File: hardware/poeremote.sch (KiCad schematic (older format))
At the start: 65 parts, among them J1 3.3VDC, J2 48VDC, J3 RJ45, J4 SERIAL, J5 ISP, J6 CONN_7, J7 LAMP, P4 J?, Q1 SOT23-BEC, Q2 PNP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

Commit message: Reworking hardware into wall-switch version
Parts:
- removed J6: CONN_7, symbol CONN_7
- removed P4: J?, symbol CONN_5
- removed R43, R44: 270, symbol R
- added C10: 15uF, symbol C
- added C34: 1uf, symbol C
- added C?: 0.1uF, symbol C
- added K1: RT314024, relay-RT-C/O16A5, symbol RT314024
- added K2: CONN_3, symbol CONN_3
- added P1: CONN_2, symbol CONN_2
- added P2: CONN_10, symbol CONN_10
- added R53, R54: 47k, symbol R
- added R55: 60K, symbol R
- added Sw1, Sw2: SPST-D, symbol SPST-D
- added U6: RE200B, symbol RE200B
- added U7: ZEPIR0AAS02MOD, symbol ZEPIR0AAS02MOD
- added U8: GA1A1S, symbol GA1A1S
- C24, C6, C8: Voltage (none) -> 16V
- C4, C5: Voltage (none) -> 100V
- C9: value 15uF -> 100nF; Voltage (none) -> 100V
- R17: value 8.66K -> 5.6K
- R3: value 2.87K -> 9.424K
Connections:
- net labels added: EXT_PA2, EXT_PA3, EXT_PC4, EXT_PC5, EXT_PC6, EXT_PC7, EXT_PD0, EXT_PD1, EXT_PD2, LIGHT_V, PIR_RX, PIR_TX, sw_bottom, sw_top
- net labels removed: SR1, SR2, SR3, SR4, VCC
- wire segments 236 -> 255
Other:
- moved on the sheet: J2

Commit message: Modified the board to use correctly-sized components, re-laid it out to fit in as a light switch, upgraded to a newer version of KiCad, and used an extra field in KiCad to indicate the Mouser part number for most of the parts
The end result is that building a BOM is much easier now, to the point that you can order from mouser directly from the auto-generated BOM.
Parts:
- removed U5: XMEGA A4, symbol XMEGA~A4
- added D3, D4: LED, symbol LED
- added R56, R57: 10, symbol R
- added U5: XMEGA-A4, symbol XMEGA-A4
- C10: Mouser Part Number (none) -> 647-UUR2A220MNL1GS
- C12: footprint (none) -> SM0603; Mouser Part Number (none) -> 581-06031C102K; Voltage (none) -> 100
- C13, C14, C15, C16, C17, C18, C19, C20: Mouser Part Number (none) -> 581-06031C102K
- C21: Mouser Part Number (none) -> 603-CC805MKX5R5BB226; Voltage (none) -> 6.3V
- C22: Mouser Part Number (none) -> 77-VJ0603Y332KXACBC; Voltage (none) -> 16
- C23: Mouser Part Number (none) -> 77-VJ0603Y332KXACBC; Voltage (none) -> 16V
- C24: Mouser Part Number (none) -> 810-C1608X5R1C334K
- C25: Mouser Part Number (none) -> 598-AVE108M10G24T-F; Voltage (none) -> 6.3V
- C27, C28, C29, C33: Mouser Part Number (none) -> 581-060316C104K
- C30: Mouser Part Number (none) -> 603-CC603MRX5R5BB106
- C31, C32: Mouser Part Number (none) -> 810-C1608C0G1H180J
- C34: Mouser Part Number (none) -> 77-VJ0603V105MXQPBC
- C35: renamed from C?; Mouser Part Number (none) -> 581-060316C104K
- C4, C5, C9: Mouser Part Number (none) -> 603-CC206KKX7R0BB104
- C6: Mouser Part Number (none) -> 77-VJ0603V104ZXAPBC
- C8: Mouser Part Number (none) -> 77-VJ0603Y151KXACBC
- D1: Mouser Part Number (none) -> 863-MBRS1100T3G
- D2: Mouser Part Number (none) -> 625-BZT52C5V1-V
- J3: Mouser Part Number (none) -> 523-RJHSE-3081
- J5: Mouser Part Number (none) -> 649-78548-406HLF
- L1, L3: Mouser Part Number (none) -> 81-BLM21P300S
- L2: Mouser Part Number (none) -> 652-SDR0805-330KL
- Q1: Mouser Part Number (none) -> 512-MMBT3904
- Q2: Mouser Part Number (none) -> 771-BCW89215
- R1: Mouser Part Number (none) -> 667-ERJ-3EKF1002V
- R10: Mouser Part Number (none) -> 667-ERJ-3EKF3012V
- R11: Mouser Part Number (none) -> 302-45.3-RC
- R12: Mouser Part Number (none) -> 301-5.1-RC
- R17: value 5.6K -> 9.424K; Mouser Part Number (none) -> 667-ERJ-3EKF9531V
- R3: value 9.424K -> 5.6K; Mouser Part Number (none) -> 279-CFR25J5K6
- R40: Mouser Part Number (none) -> 302-2.32K-RC
- R41, R42: Mouser Part Number (none) -> 301-220-RC
- R45: value 270 -> 220; Mouser Part Number (none) -> 301-220-RC
- R47, R48, R49, R50: Mouser Part Number (none) -> 301-51-RC
- R51: value 100K -> 25.5k; Mouser Part Number (none) -> 667-ERJ-3EKF2552V
- R52: value 50K -> 25.5k; Mouser Part Number (none) -> 667-ERJ-3EKF2552V
- R53, R54: Mouser Part Number (none) -> 667-ERJ-3GEYJ473V
- R55: value 60K -> 47k; Mouser Part Number (none) -> 667-ERJ-3GEYJ473V
- R6: Mouser Part Number (none) -> 667-ERJ-3EKF2552V
- Sw1, Sw2: Mouser Part Number (none) -> 101-0624-EV
- T1: Mouser Part Number (none) -> 871-B78476A8248A3
- U3: Mouser Part Number (none) -> 634-SI3402-A-GM
- U4: Mouser Part Number (none) -> 579-ENC28J60-I/SS
- U6: Mouser Part Number (none) -> -
- U7: Mouser Part Number (none) -> 692-ZMOT0BSB1A0CG
- U8: Mouser Part Number (none) -> 852-GA1A1S202WP
- X1: Mouser Part Number (none) -> 815-ABM3C-25-D4YT
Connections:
- net labels added: EXT_PB3, SLED1, SLED2
- wire segments 255 -> 258

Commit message: Fixed the PIR motion nsensor
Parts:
- removed R53: 47k, symbol R
- removed U7: ZEPIR0AAS02MOD, symbol ZEPIR0AAS02MOD
- added C11, C3: 10uf, symbol C
- added C2: 100uF, symbol C
- added C26, C7: 10nF, symbol C
- added R13, R14: 100k, symbol R
- added R15, R7: 1M, symbol R
- added R4, R5, R8, R9: 10k, symbol R
- added U1: LM358, symbol LM358
- C1: renamed from C34; value 1uf -> 10uf
- renumbered R54 to R2
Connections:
- net labels added: EXT_PC2, EXT_PC3, MOT_NEG, MOT_POS
- net labels removed: PIR_RX, PIR_TX
- wire segments 258 -> 281
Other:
- moved on the sheet: C1, R2, U6

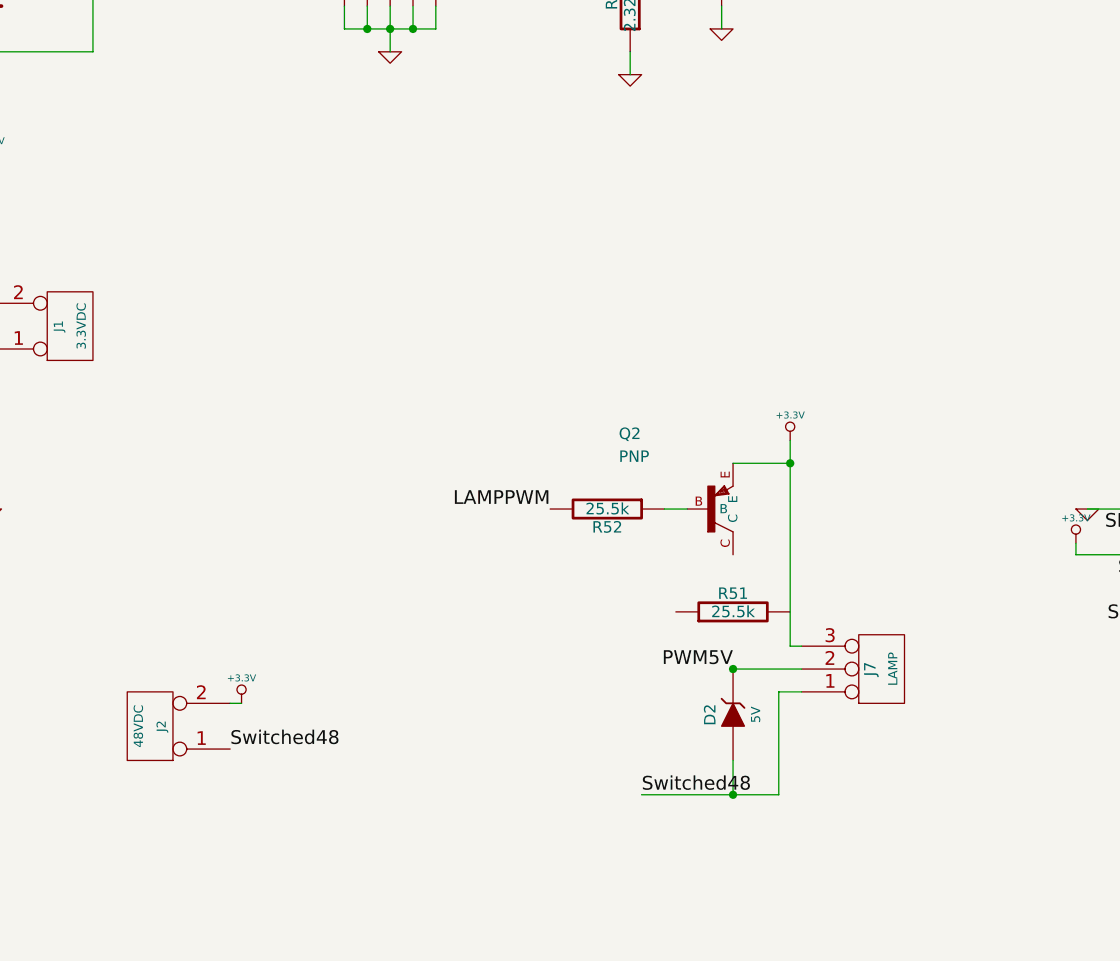
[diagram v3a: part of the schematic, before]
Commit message: Redid the board to include an open-loop mini dc-dc converter run by the xmega
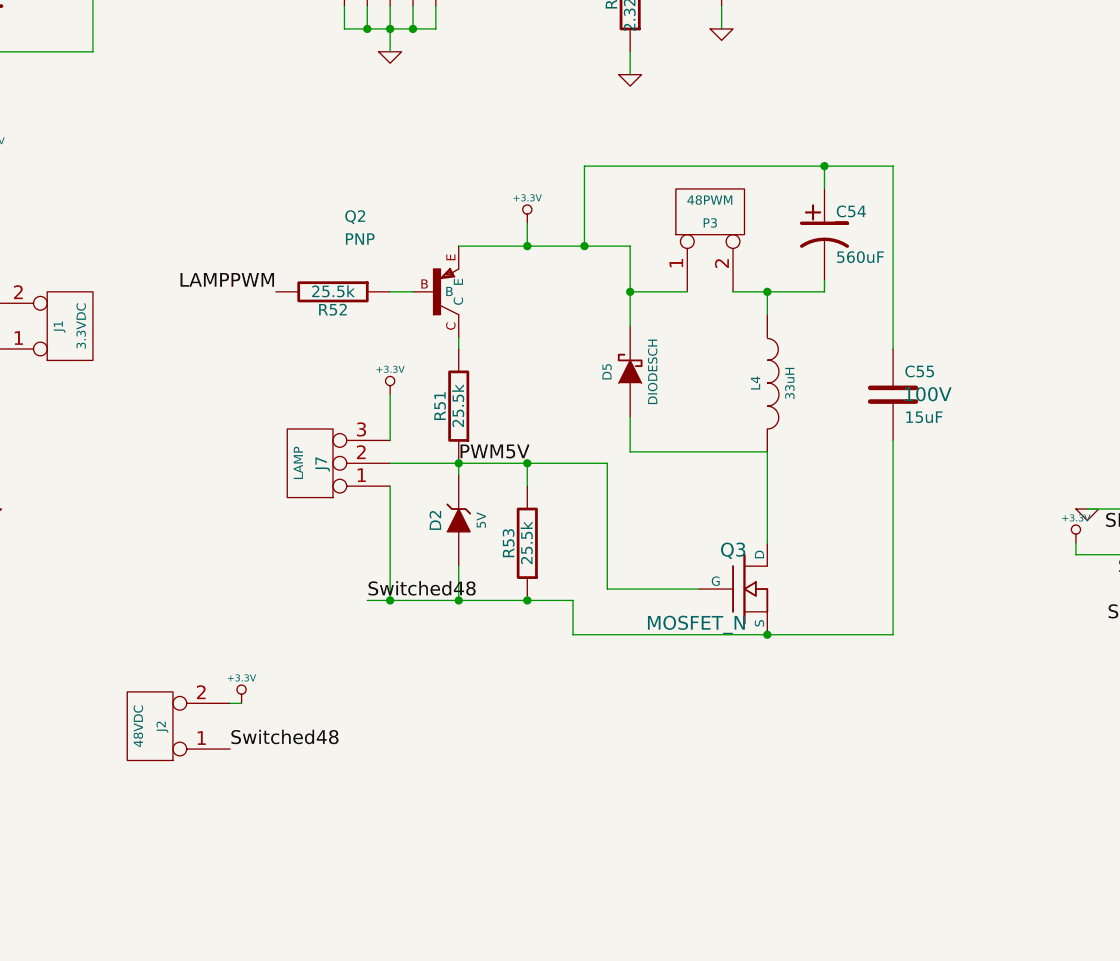
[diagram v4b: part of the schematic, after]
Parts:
- added C54: 560uF, symbol CP1
- added C55: 15uF, symbol C
- added D5: DIODESCH, symbol DIODESCH
- added L4: 33uH, symbol INDUCTOR
- added P3: 48PWM, symbol CONN_2
- added Q3: MOSFET_N, symbol MOSFET_N
- added R53: 25.5k, symbol R
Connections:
- wire segments 281 -> 300
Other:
- moved on the sheet: D2, J7, Q2, R51, R52

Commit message: changes to the schematic, not yet in board.
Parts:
- removed R45: 220, symbol R
- C1, C11, C3: Mouser Part Number 77-VJ0603V105MXQPBC -> 603-CC603MRX5R5BB106
- C2: value 100uF -> 22uF; Mouser Part Number 77-VJ0603V105MXQPBC -> 810-C1608X5R0J226M
- C25: Mouser Part Number 598-AVE108M10G24T-F -> 647-UCD0J102MNL1GS
- C26, C7: Mouser Part Number 77-VJ0603V105MXQPBC -> GRM188R71H103JA01D
- Q3: Mouser Part Number (none) -> 942-IRLML2060TRPBF
- R13, R14: Mouser Part Number 667-ERJ-3GEYJ473V -> 603-AC0603JR-07100KL
- R15, R7: Mouser Part Number 667-ERJ-3GEYJ473V -> 603-AC0603JR-071ML
- R17: value 9.424K -> 3.327K
- R4, R5, R8, R9: Mouser Part Number 667-ERJ-3GEYJ473V -> 667-ERJ-3EKF1002V
- U1: Mouser Part Number (none) -> 595-LM358ADRE4
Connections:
- net labels added: ETHCS
- net labels removed: ETHEN
- wire segments 300 -> 299
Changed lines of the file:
@@
-EESchema Schematic File Version 2  date Sun 08 Jul 2012 11:13:59 PM EDT
+EESchema Schematic File Version 2  date Sat 26 Jan 2013 07:09:22 PM EST
 LIBS:power
 LIBS:device
@@
 EELAYER END
 $Descr A4 11700 8267
-encoding utf-8
 Sheet 1 1
 Title ""
-Date "9 jul 2012"
+Date "27 jan 2013"
 Rev ""
 Comp ""
@@
 Comment4 ""
 $EndDescr
+Text Label 16000 2250 0    60   ~ 0
+ETHCS
 Connection ~ 10500 4850
 Wire Wire Line
@@
 Wire Wire Line
 	9750 2900 10050 2900
-Wire Wire Line
-	10550 2850 10550 2900
 Wire Wire Line
 	10300 3600 10300 3700
@@
 F 0 "Q3" H 10410 6320 60  0000 R CNN
 F 1 "MOSFET_N" H 10410 6000 60  0000 R CNN
+F 4 "942-IRLML2060TRPBF" H 10400 6150 60  0001 C CNN "Mouser Part Number"
 	1    10400 6150
 	1    0    0    -1
@@
 F 0 "C26" H 23500 3950 50  0000 L CNN
 F 1 "10nF" H 23500 3750 50  0000 L CNN
-F 4 "77-VJ0603V105MXQPBC" H 23450 3850 60  0001 C CNN "Mouser Part Number"
+F 4 "GRM188R71H103JA01D" H 23450 3850 60  0001 C CNN "Mouser Part Number"
 	1    23450 3850
 	0    -1   -1   0
@@
 F 0 "R15" V 23530 3550 50  0000 C CNN
 F 1 "1M" V 23450 3550 50  0000 C CNN
-F 4 "667-ERJ-3GEYJ473V" H 23450 3550 60  0001 C CNN "Mouser Part Number"
+F 4 "603-AC0603JR-071ML" H 23450 3550 60  0001 C CNN "Mouser Part Number"
 	1    23450 3550
 	0    -1   1    0
@@
 F 0 "R13" V 22530 2800 50  0000 C CNN
 F 1 "100k" V 22450 2800 50  0000 C CNN
-F 4 "667-ERJ-3GEYJ473V" H 22450 2800 60  0001 C CNN "Mouser Part Number"
+F 4 "603-AC0603JR-07100KL" H 22450 2800 60  0001 C CNN "Mouser Part Number"
 	1    22450 2800
 	-1   0    0    -1
@@
 F 0 "R14" V 22530 3800 50  0000 C CNN
 F 1 "100k" V 22450 3800 50  0000 C CNN
-F 4 "667-ERJ-3GEYJ473V" H 22450 3800 60  0001 C CNN "Mouser Part Number"
+F 4 "603-AC0603JR-07100KL" H 22450 3800 60  0001 C CNN "Mouser Part Number"
 	1    22450 3800
 	-1   0    0    -1
@@
 F 0 "R9" V 21930 3900 50  0000 C CNN
 F 1 "10k" V 21850 3900 50  0000 C CNN
-F 4 "667-ERJ-3GEYJ473V" H 21850 3900 60  0001 C CNN "Mouser Part Number"
+F 4 "667-ERJ-3EKF1002V" H 21850 3900 60  0001 C CNN "Mouser Part Number"
 	1    21850 3900
 	-1   0    0    -1
@@
 F 0 "R8" V 21930 3300 50  0000 C CNN
 F 1 "10k" V 21850 3300 50  0000 C CNN
-F 4 "667-ERJ-3GEYJ473V" H 21850 3300 60  0001 C CNN "Mouser Part Number"
+F 4 "667-ERJ-3EKF1002V" H 21850 3300 60  0001 C CNN "Mouser Part Number"
 	1    21850 3300
 	-1   0    0    -1
@@
 F 0 "R7" V 21430 3600 50  0000 C CNN
 F 1 "1M" V 21350 3600 50  0000 C CNN
-F 4 "667-ERJ-3GEYJ473V" H 21350 3600 60  0001 C CNN "Mouser Part Number"
+F 4 "603-AC0603JR-071ML" H 21350 3600 60  0001 C CNN "Mouser Part Number"
 	1    21350 3600
 	0    -1   1    0
@@
 F 0 "C7" H 21400 4050 50  0000 L CNN
 F 1 "10nF" H 21400 3850 50  0000 L CNN
-F 4 "77-VJ0603V105MXQPBC" H 21350 3950 60  0001 C CNN "Mouser Part Number"
+F 4 "GRM188R71H103JA01D" H 21350 3950 60  0001 C CNN "Mouser Part Number"
 	1    21350 3950
 	0    -1   -1   0
@@
 F 0 "C3" H 20600 4100 50  0000 L CNN
 F 1 "10uf" H 20600 3900 50  0000 L CNN
-F 4 "77-VJ0603V105MXQPBC" H 20550 4000 60  0001 C CNN "Mouser Part Number"
+F 4 "603-CC603MRX5R5BB106" H 20550 4000 60  0001 C CNN "Mouser Part Number"
 	1    20550 4000
 	1    0    0    -1
@@
 F 0 "R5" V 20630 3550 50  0000 C CNN
 F 1 "10k" V 20550 3550 50  0000 C CNN
-F 4 "667-ERJ-3GEYJ473V" H 20550 3550 60  0001 C CNN "Mouser Part Number"
+F 4 "667-ERJ-3EKF1002V" H 20550 3550 60  0001 C CNN "Mouser Part Number"
 	1    20550 3550
 	-1   0    0    -1
@@
 F 0 "C11" H 22100 3500 50  0000 L CNN
 F 1 "10uf" H 22100 3300 50  0000 L CNN
-F 4 "77-VJ0603V105MXQPBC" H 22050 3400 60  0001 C CNN "Mouser Part Number"
+F 4 "603-CC603MRX5R5BB106" H 22050 3400 60  0001 C CNN "Mouser Part Number"
 	1    22050 3400
 	1    0    0    -1
@@
 F 0 "R4" V 20030 2450 50  0000 C CNN
 F 1 "10k" V 19950 2450 50  0000 C CNN
-F 4 "667-ERJ-3GEYJ473V" H 19950 2450 60  0001 C CNN "Mouser Part Number"
+F 4 "667-ERJ-3EKF1002V" H 19950 2450 60  0001 C CNN "Mouser Part Number"
 	1    19950 2450
 	0    -1   1    0
@@
 P 20200 2650
 F 0 "C2" H 20250 2750 50  0000 L CNN
-F 1 "100uF" H 20250 2550 50  0000 L CNN
-F 4 "77-VJ0603V105MXQPBC" H 20200 2650 60  0001 C CNN "Mouser Part Number"
+F 1 "22uF" H 20250 2550 50  0000 L CNN
+F 4 "810-C1608X5R0J226M" H 20200 2650 60  0001 C CNN "Mouser Part Number"
 	1    20200 2650
 	1    0    0    -1
@@
 F 0 "U1" H 21000 3250 60  0000 L CNN
 F 1 "LM358" H 21000 2800 60  0000 L CNN
+F 4 "595-LM358ADRE4" H 21050 3050 60  0001 C CNN "Mouser Part Number"
 	1    21050 3050
 	1    0    0    -1
@@
 Text Label 16000 2550 0    60   ~ 0
 EXT_PD1
-Text Label 16000 2450 0    60   ~ 0
+Text Label 16700 2400 0    60   ~ 0
 EXT_PD2
 Text Label 16650 5700 2    60   ~ 0
@@
 	1    0    0    -1
 $EndComp
-Text Label 16000 2350 0    60   ~ 0
+Text Label 16000 2450 0    60   ~ 0
 sw_bottom
 Text Label 13800 750  1    60   ~ 0
@@
 F 0 "C1" H 19750 2750 50  0000 L CNN
 F 1 "10uf" H 19750 2550 50  0000 L CNN
-F 4 "77-VJ0603V105MXQPBC" H 19700 2650 60  0001 C CNN "Mouser Part Number"
+F 4 "603-CC603MRX5R5BB106" H 19700 2650 60  0001 C CNN "Mouser Part Number"
 	1    19700 2650
 	1    0    0    -1
@@
 F 1 "+3.3V" H 8850 1910 30  0000 C CNN
 	1    8850 1800
-	1    0    0    -1
-$EndComp
-$Comp
-L +3.3V #PWR023
-U 1 1 4E781610
-P 10550 2850
-F 0 "#PWR023" H 10550 2810 30  0001 C CNN
-F 1 "+3.3V" H 10550 2960 30  0000 C CNN
-	1    10550 2850
 	1    0    0    -1
 $EndComp
@@
 Text Label 10550 2350 0    60   ~ 0
 ETHRST
-$Comp
-L R R45
-U 1 1 4E7814FC
-P 10300 2900
-F 0 "R45" V 10380 2900 50  0000 C CNN
-F 1 "220" V 10300 2900 50  0000 C CNN
-F 4 "301-220-RC" H 10300 2900 60  0001 C CNN "Mouser Part Number"
-	1    10300 2900
-	0    -1   -1   0
-$EndComp
-Text Label 10700 3000 0    60   ~ 0
-ETHEN
+Text Label 10050 2900 0    60   ~ 0
+ETHCS
 $Comp
 L CP1 C30
@@
 	1    0    0    -1
 $EndComp
-Text Label 16000 2250 0    60   ~ 0
+Text Label 16000 2350 0    60   ~ 0
 ETHINT
 Text Label 9750 2200 0    60   ~ 0
@@
 F 0 "C25" H 5400 5250 50  0000 L CNN
 F 1 "560uF" H 5400 5050 50  0000 L CNN
-F 4 "598-AVE108M10G24T-F" H 5350 5150 60  0001 C CNN "Mouser Part Number"
+F 4 "647-UCD0J102MNL1GS" H 5350 5150 60  0001 C CNN "Mouser Part Number"
 F 5 "6.3V" H 5350 5150 60  0001 C CNN "Voltage"
 	1    5350 5150
@@
 P 6550 5350
 F 0 "R17" V 6630 5350 50  0000 C CNN
-F 1 "9.424K" V 6550 5350 50  0000 C CNN
+F 1 "3.327K" V 6550 5350 50  0000 C CNN
 F 4 "667-ERJ-3EKF9531V" H 6550 5350 60  0001 C CNN "Mouser Part Number"
 	1    6550 5350

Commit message: Added the display, maybe ready to make v2.2 boards
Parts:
- removed C54: 560uF, symbol CP1
- removed C55: 15uF, symbol C
- removed D5: DIODESCH, symbol DIODESCH
- removed J2: 48VDC, symbol CONN_2
- removed K1: RT314024, relay-RT-C/O16A5, symbol RT314024
- removed K2: CONN_3, symbol CONN_3
- removed L4: 33uH, symbol INDUCTOR
- removed P1: CONN_2, symbol CONN_2
- removed P3: 48PWM, symbol CONN_2
- removed Q3: MOSFET_N, symbol MOSFET_N
- added AFF1: DC08-11, symbol DC08-11
- added P1: CONN_5, symbol CONN_5
- added R17, R18, R19, R20, R21, R22, R23, R24, R25, R26, R27, R28, R29, R30, R31, R32: 50, symbol R
- C1, C11, C3, C30: MPN (none) -> C0805C106M9PACTU; Supplier (none) -> Avnet
- C10: MPN (none) -> EEE-TG2A220UP; Supplier (none) -> Avnet
- C12: Supplier (none) -> Avnet
- C13, C14, C15, C16, C17, C18, C19, C20: MPN (none) -> C0603C102K1RACTU; Supplier (none) -> Avnet
- C21: MPN (none) -> CE JMK212 BJ226MG-T; Supplier (none) -> Avnet
- C22, C23: MPN (none) -> C0603C332K5RACTU; Supplier (none) -> Avnet
- C24: MPN (none) -> GRM188R71C334KA01D; Supplier (none) -> Avnet
- C25: MPN (none) -> EEE-FK1A681AP; Supplier (none) -> Avnet
- C26, C7: MPN (none) -> C0603C103M5RAC7411; Supplier (none) -> Avnet
- C27, C28, C29, C35, C4: MPN (none) -> 12061C104KAT2A; Supplier (none) -> Avnet
- C31, C32: MPN (none) -> VJ0603A180JXACW1BC; Supplier (none) -> Avnet
- C33, C6: MPN (none) -> C0603C104K3RAC7411; Supplier (none) -> Avnet
- C5, C9: MPN (none) -> CG HMK212 B7104KG-T; Supplier (none) -> Avnet
- C8: MPN (none) -> C0603C151J5GACTU; Supplier (none) -> Avnet
- D1: MPN (none) -> MBRS1100T3G; Supplier (none) -> Avnet
- D2: MPN (none) -> BZT52C5V1-7-F; Supplier (none) -> Avnet
- J3: MPN (none) -> RJHSE3381; Mouser Part Number 523-RJHSE-3081 -> H1197NL; Supplier (none) -> Avnet
- J5: MPN (none) -> 78548-406HLF; Supplier (none) -> Avnet
- L1, L3: MPN (none) -> BLM21PG300SN1D; Supplier (none) -> Avnet
- L2: MPN (none) -> SDR0805-330KL; Supplier (none) -> Avnet
- Q1: MPN (none) -> MMBT3904; Supplier (none) -> Avnet
- Q2: MPN (none) -> BCW89,215; Supplier (none) -> Avnet
- R1: value 10K -> 10k; MPN (none) -> RC1608F1002CS; Supplier (none) -> Avnet
- R10: MPN (none) -> CRCW060330K1FKEA; Supplier (none) -> Avnet
- R11: MPN (none) -> ERJ-3EKF45R3V; Supplier (none) -> Avnet
- R12: MPN (none) -> CRCW06035R10JNEA; Supplier (none) -> Avnet
- R13, R14: MPN (none) -> RC1608F1003CS; Supplier (none) -> Avnet
- R15, R7: MPN (none) -> CRCW06031M00JNEA; Supplier (none) -> Avnet
- R16: renamed from R17; MPN (none) -> CRCW06033K32FKEA; Supplier (none) -> Avnet
- R2, R55: MPN (none) -> CRCW060347K0JNEA; Supplier (none) -> Avnet
- R3: MPN (none) -> ERJ-3EKF5601V; Supplier (none) -> Avnet
- R4, R5, R8, R9: MPN (none) -> RC1608F1002CS; Supplier (none) -> Avnet
- R40: MPN (none) -> CRCW06032K32FKEA; Supplier (none) -> Avnet
- R41, R42: MPN (none) -> ERJ-3GEYJ224V; Supplier (none) -> Avnet
- R47, R48, R49, R50: MPN (none) -> ERJ-3EKF51R0V; Supplier (none) -> Avnet
- R51, R52, R53: MPN (none) -> ERJ-3EKF2552V; Supplier (none) -> Avnet
- R56, R57: MPN (none) -> CRCW060310R0JNEA; Supplier (none) -> Avnet
- R6: value 25.5K -> 25.5k; MPN (none) -> ERJ-3EKF2552V; Supplier (none) -> Avnet
- Sw1, Sw2: MPN (none) -> 101-0624-EV; Supplier (none) -> Mouser
- T1: MPN (none) -> H2019NL; Supplier (none) -> Avnet
- U1: MPN (none) -> LM358AD; Mouser Part Number 595-LM358ADRE4 -> (none); Supplier (none) -> Avnet
- U3: MPN (none) -> SI3402-A-GM; Supplier (none) -> Avnet
- U4: MPN (none) -> ENC28J60/SS; Supplier (none) -> Avnet
- U5: MPN (none) -> ATXMEGA32A4U-AU; Supplier (none) -> Avnet
- X1: MPN (none) -> FQ5032B-25.000; Supplier (none) -> Avnet
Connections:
- net labels added: EXT_PA4, EXT_PA5, EXT_PA6, EXT_PB2, EXT_PC0, EXT_PC1, motion_firstfilter, motion_output, motion_power, switchedout, vfeedback
- net labels removed: EXT_PC2, EXT_PC3
- wire segments 299 -> 278
